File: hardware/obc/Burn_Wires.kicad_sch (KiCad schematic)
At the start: 28 parts, among them Q10 IRF7406PbF, Q20 IRLML2803, Q21 IRF7406PbF, Q4 IRLML2803, Q5 IRLML2803, Q6 MMBT2222AT, Q9 IRF7406PbF, U16 PE014006

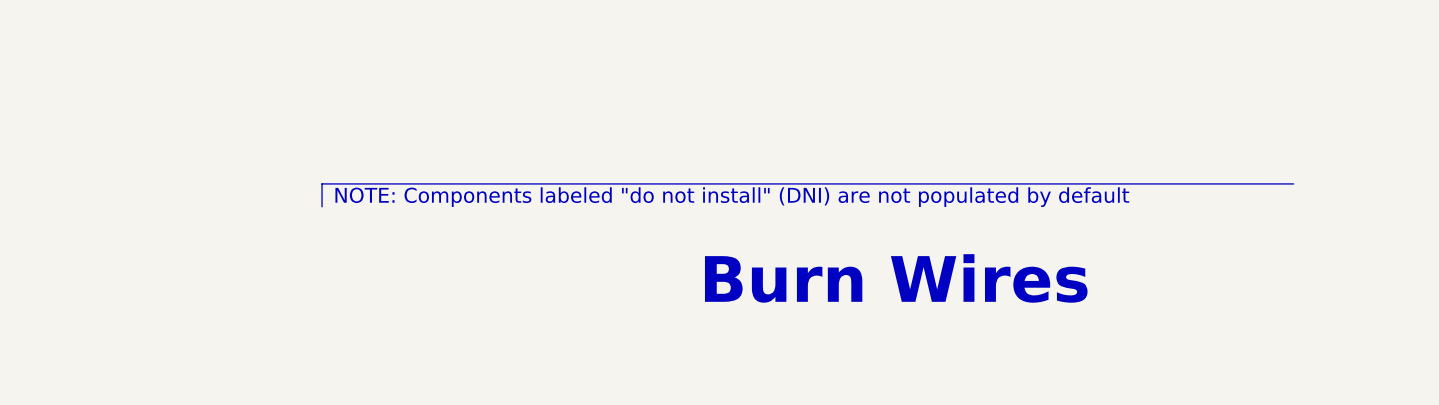
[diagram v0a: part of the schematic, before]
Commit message: obc: Schematic pages to US Letter (except Power)
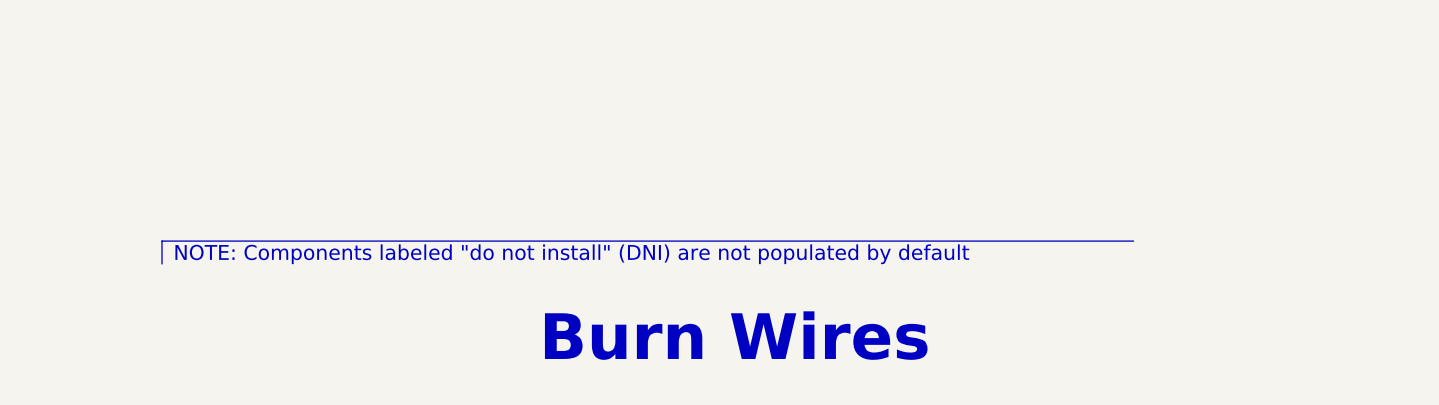
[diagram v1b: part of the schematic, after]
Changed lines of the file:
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@@
 	(generator "eeschema")
 	(generator_version "8.0")
-	(paper "A4")
+	(paper "USLetter")
 	(title_block
 		(title "PyCubed Mainboard")
@@
 	(polyline
 		(pts
-			(xy 176.53 165.1) (xy 176.53 162.56)
+			(xy 158.75 171.45) (xy 158.75 168.91)
 		)
 		(stroke
@@
 	(polyline
 		(pts
-			(xy 176.53 162.56) (xy 284.48 162.56)
+			(xy 158.75 168.91) (xy 266.7 168.91)
 		)
 		(stroke
@@
 	(text "Burn Wires"
 		(exclude_from_sim no)
-		(at 218.44 176.53 0)
+		(at 200.66 182.88 0)
 		(effects
 			(font
@@
 	(text "NOTE: Components labeled \"do not install\" (DNI) are not populated by default"
 		(exclude_from_sim no)
-		(at 177.8 165.1 0)
+		(at 160.02 171.45 0)
 		(effects
 			(font

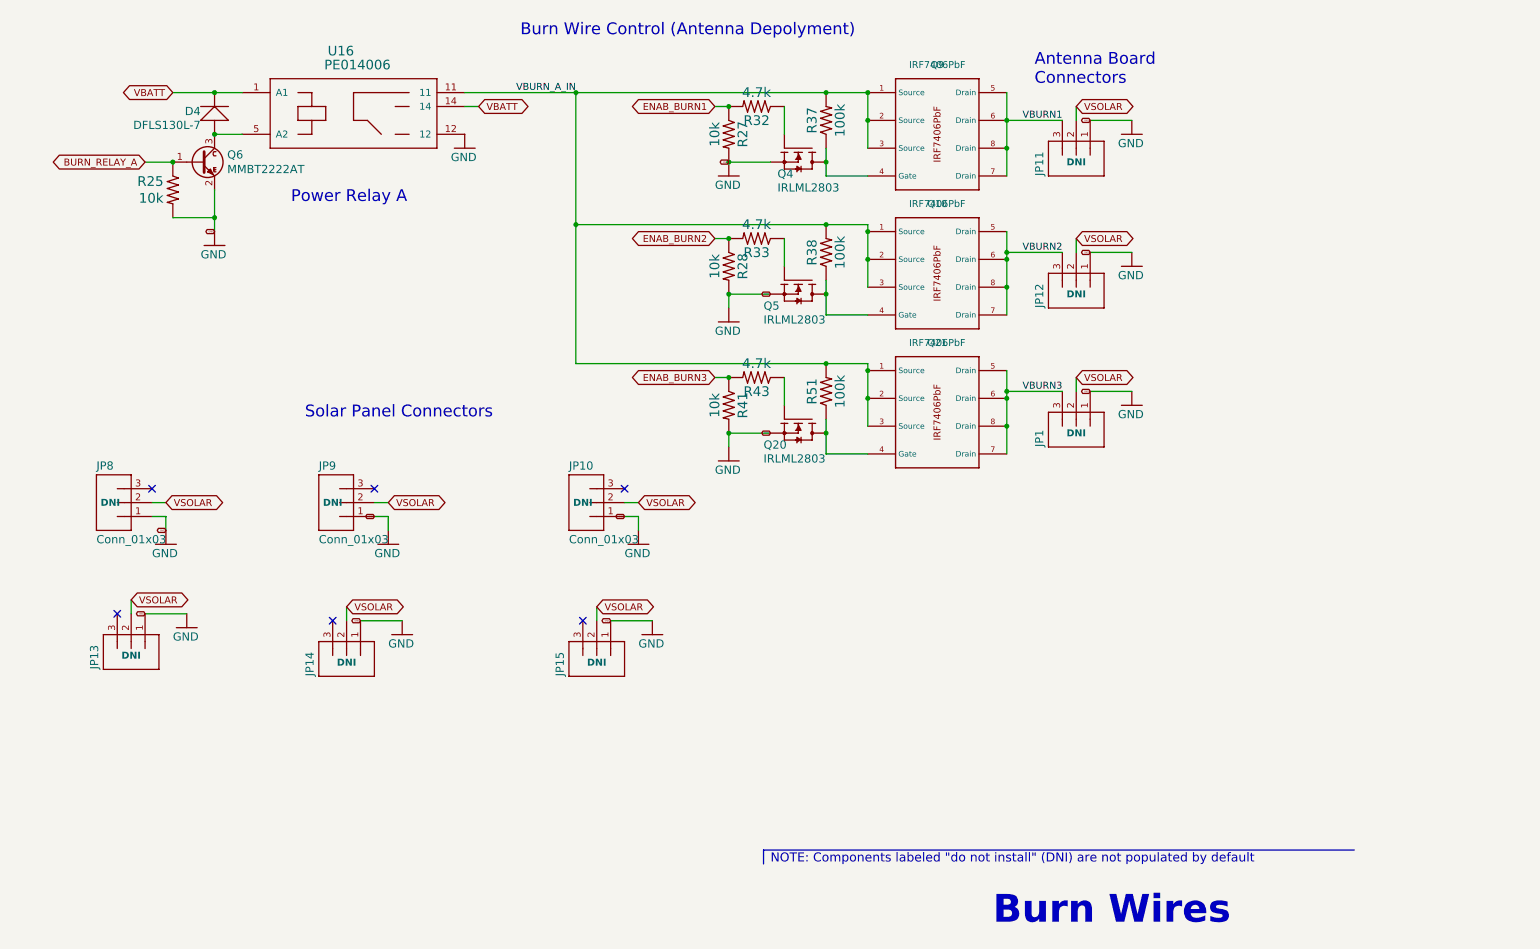
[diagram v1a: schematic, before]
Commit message: obc: schematic editing and footprint development
Deleted irrelevant SD-related circuits and pins. Created new & modified existing connector and inductor footprints. Added new components (Bat Charger, High-Rel Connector, etc.)
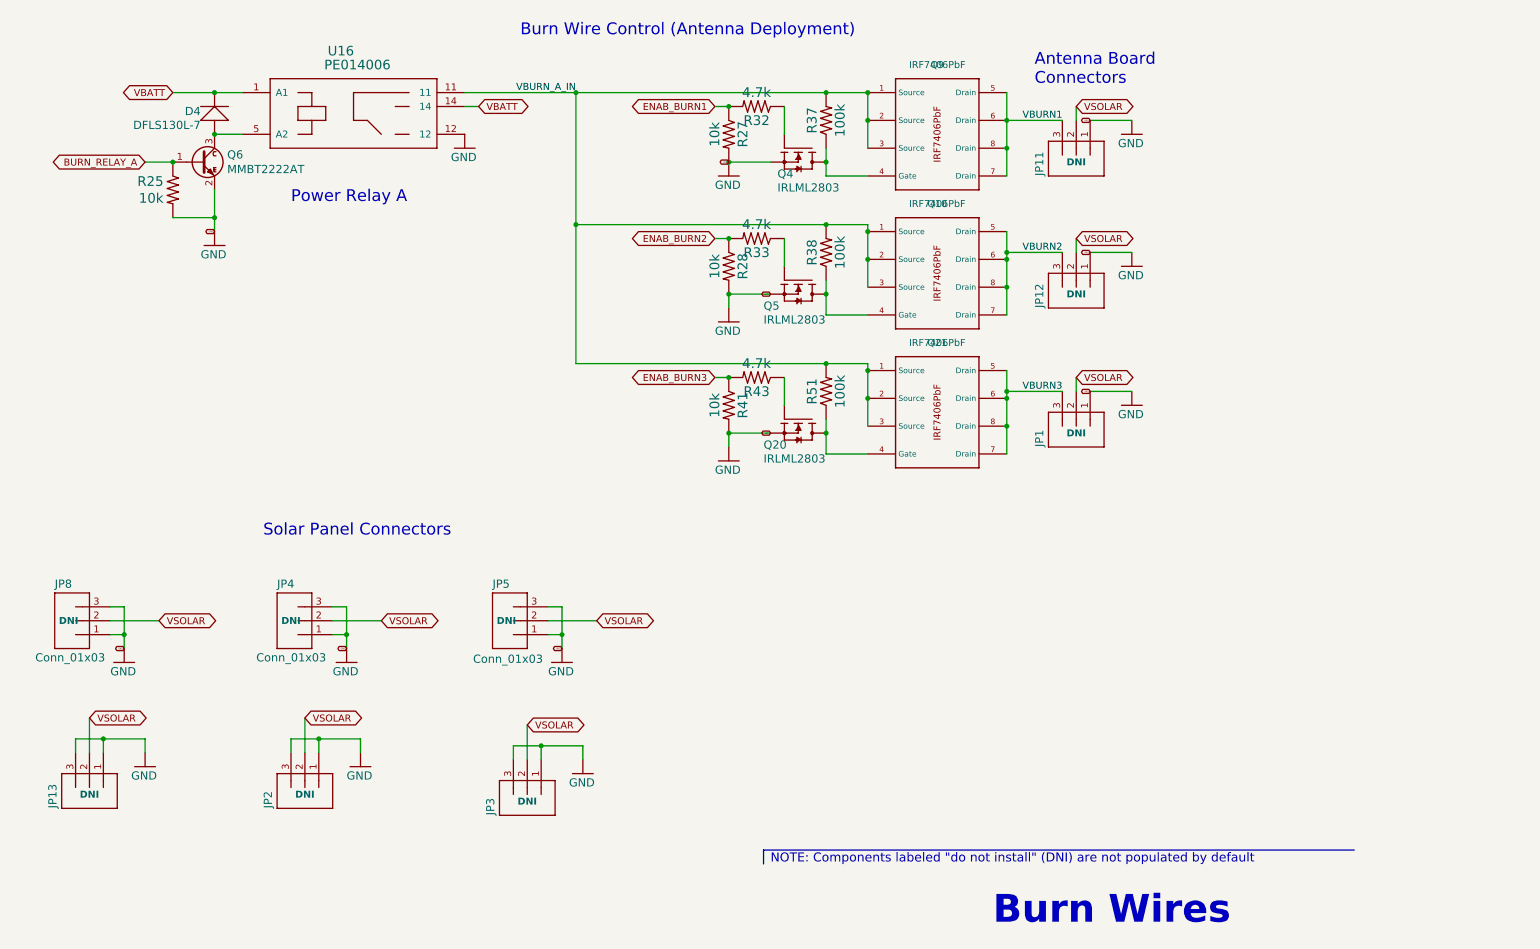
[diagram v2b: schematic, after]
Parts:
- removed JP10, JP14, JP15, JP9: Conn_01x03, mainboard:MOLEX-1X3_LOCK, symbol mainboard:M03POLAR_LOCK
- added JP2, JP3, JP4, JP5: Conn_01x03, mainboard:MOLEX-1X3_LOCK, symbol mainboard:M03POLAR_LOCK
- Q10, Q21, Q9: footprint (none) -> SSE_Footprints:SO-8_3.9x4.9mm_P1.27mm
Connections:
- net GND: now also JP13.3, JP8.3, JP2.1, JP2.3, JP3.1, JP3.3, JP4.1, JP4.3, JP5.1, JP5.3
- net VSOLAR: now also JP2.2, JP3.2, JP4.2, JP5.2
- no-connect marks 6 -> 0
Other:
- note added: "Burn Wire Control (Antenna Deployment)"
- note removed: "Burn Wire Control (Antenna Depolyment)"
- moved on the sheet: JP13, JP8

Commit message: obc: BOM component verification
Verified part numbers, availability, values, footprints, etc. of components. Next steps involve verifying footprints and potentially researching some alternative components.
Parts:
- Q10, Q21, Q9: footprint SSE_Footprints:SO-8_3.9x4.9mm_P1.27mm -> Package_SO:SO-8_3.9x4.9mm_P1.27mm
- Q20, Q4, Q5: footprint mainboard:SOT-23 -> Package_TO_SOT_SMD:SOT-23
- U16: Notes (none) -> (Potentially) Not placed by JLCPCB

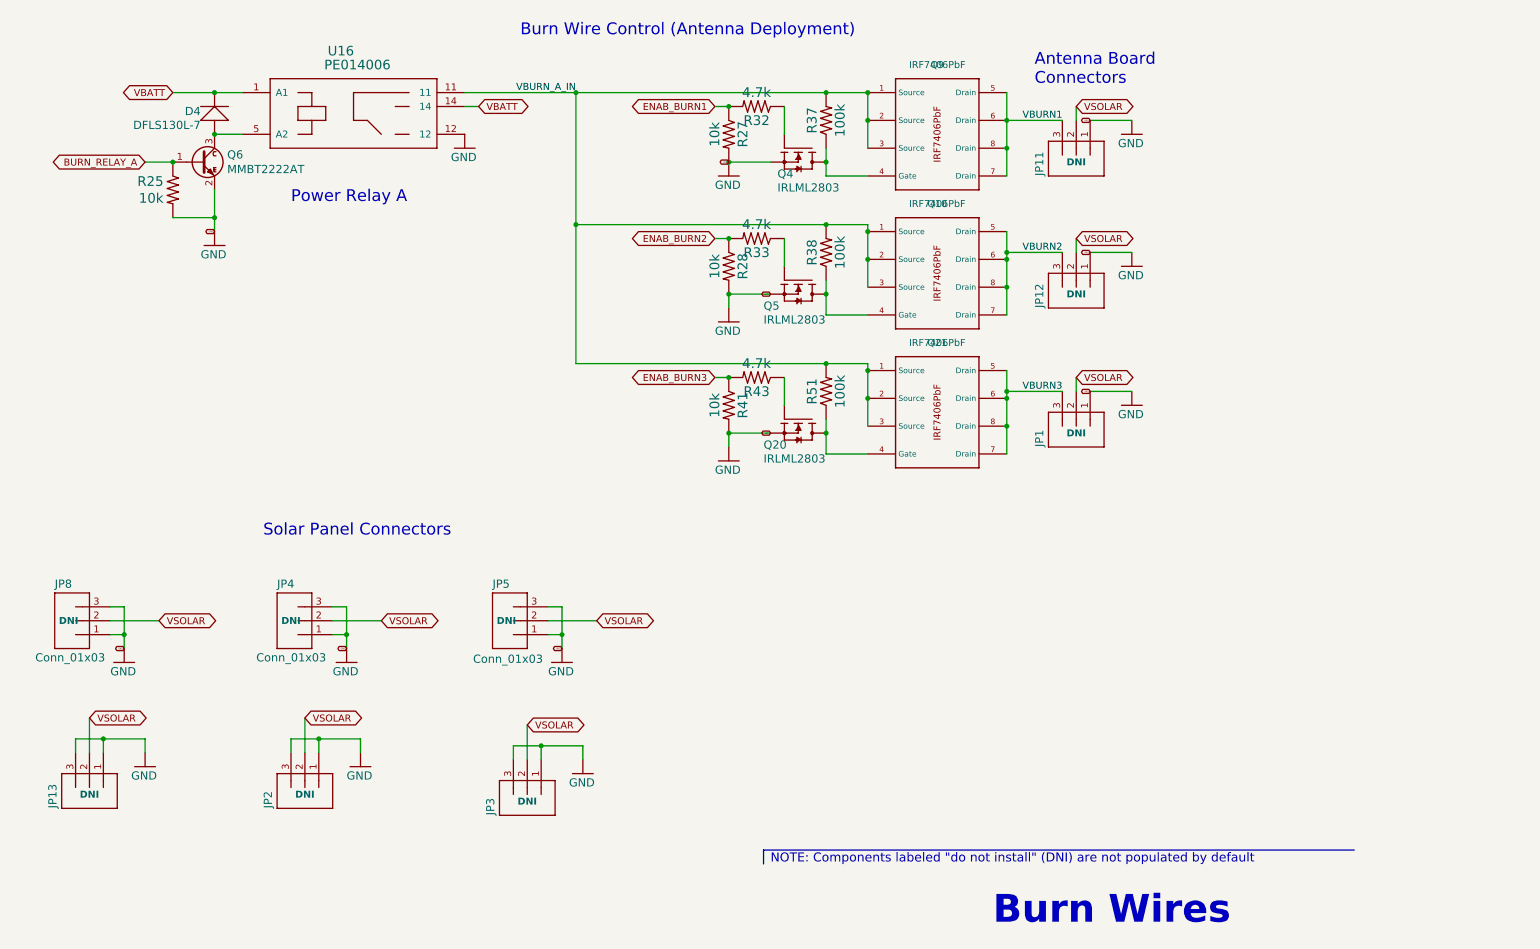
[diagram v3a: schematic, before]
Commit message: obc: footprint editing and schematic revision
Added GPS21+ and edited inductor footprints. Edited schematic circuitry and re-annotated schematic components.
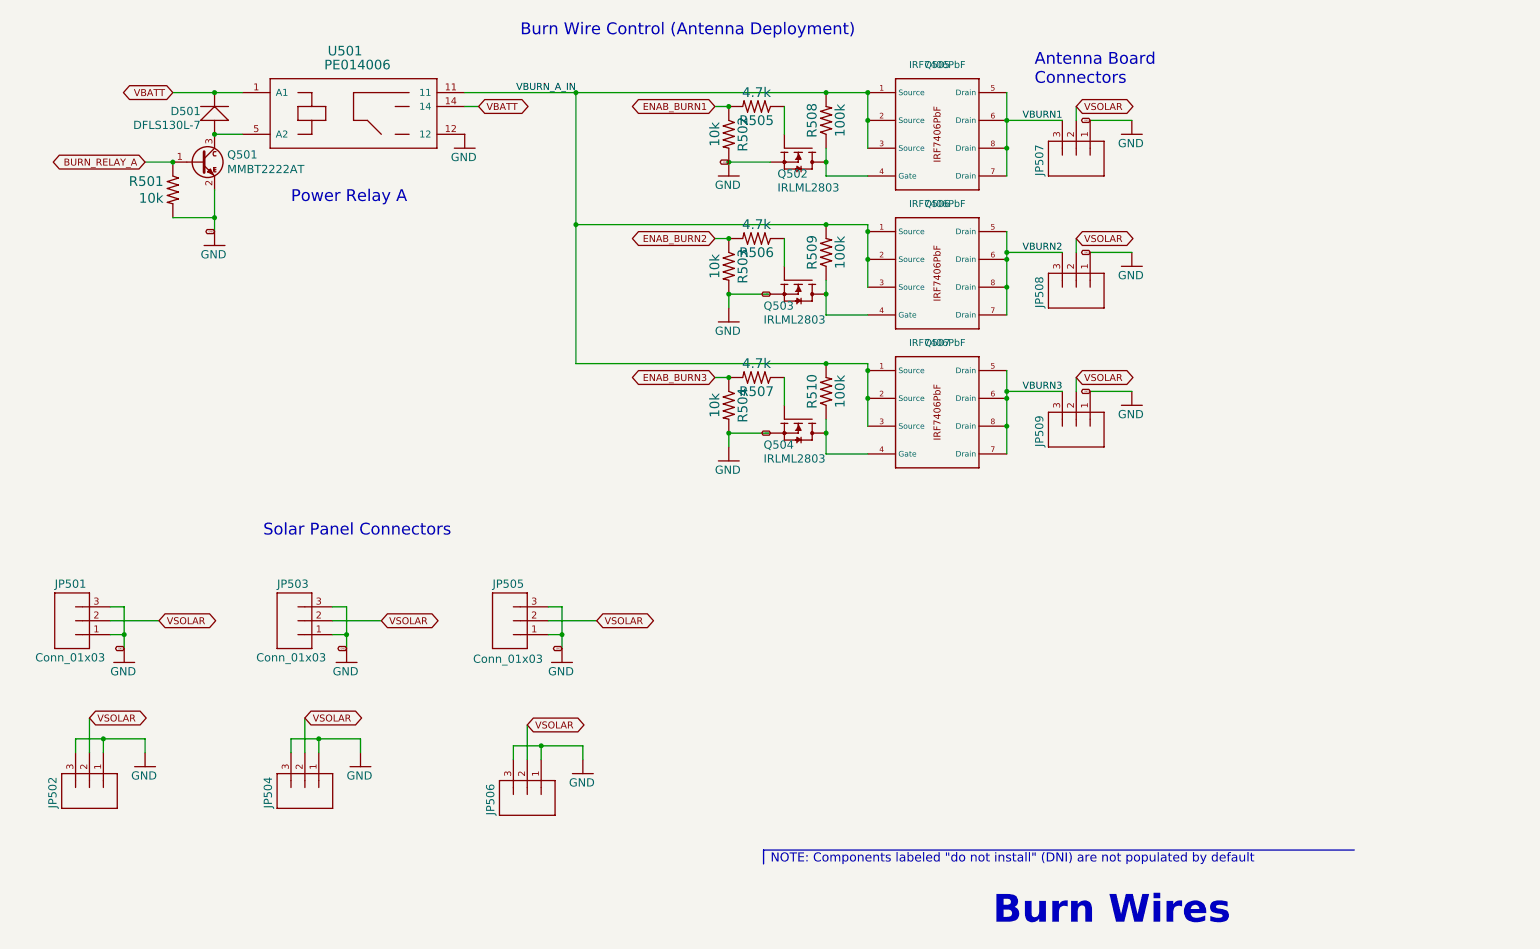
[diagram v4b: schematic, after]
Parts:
- JP501: renamed from JP8; DNI DNI -> (none); LCSC NotAvailable -> (none)
- JP502: renamed from JP13; DNI DNI -> (none); LCSC NotAvailable -> (none)
- JP503: renamed from JP4; DNI DNI -> (none); LCSC NotAvailable -> (none)
- JP504: renamed from JP2; DNI DNI -> (none); LCSC NotAvailable -> (none)
- JP505: renamed from JP5; DNI DNI -> (none); LCSC NotAvailable -> (none)
- JP506: renamed from JP3; DNI DNI -> (none); LCSC NotAvailable -> (none)
- JP507: renamed from JP11; DNI DNI -> (none); LCSC NotAvailable -> (none)
- JP508: renamed from JP12; DNI DNI -> (none); LCSC NotAvailable -> (none)
- JP509: renamed from JP1; DNI DNI -> (none); LCSC NotAvailable -> (none)
- renumbered D4 to D501, Q6 to Q501, Q4 to Q502, Q5 to Q503, Q20 to Q504, Q9 to Q505, Q10 to Q506, Q21 to Q507, R25 to R501, R27 to R502, R28 to R503, R41 to R504, R32 to R505, R33 to R506, R43 to R507, R37 to R508, R38 to R509, R51 to R510, U16 to U501

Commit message: obc: BOM editing
Edited the DNI status of several components to be more reflective of our obc setup plans.
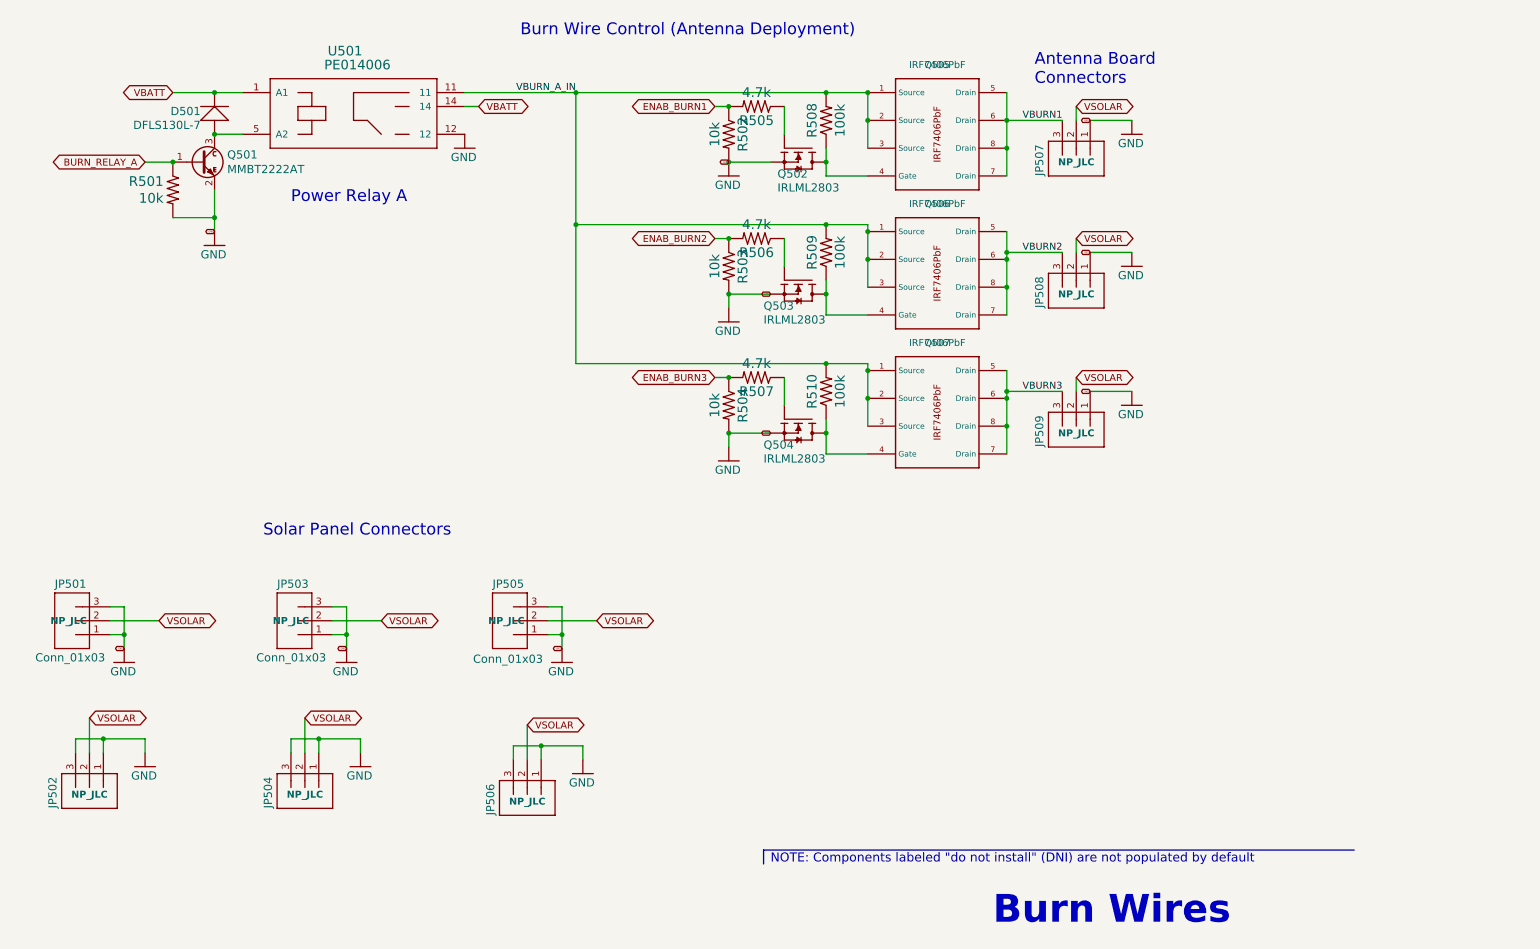
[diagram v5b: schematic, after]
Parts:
- JP501, JP502, JP503, JP504, JP505, JP506, JP507, JP508, JP509: DNI (none) -> NP_JLC
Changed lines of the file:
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@@
 			)
 		)
-		(property "DNI" ""
+		(property "DNI" "NP_JLC"
 			(at 215.9 67.31 90)
 			(effects
@@
 			)
 		)
-		(property "DNI" ""
+		(property "DNI" "NP_JLC"
 			(at 215.9 43.18 90)
 			(effects
@@
 			)
 		)
-		(property "DNI" ""
+		(property "DNI" "NP_JLC"
 			(at 35.56 158.75 90)
 			(effects
@@
 			)
 		)
-		(property "DNI" ""
+		(property "DNI" "NP_JLC"
 			(at 31.75 127 0)
 			(effects
@@
 			)
 		)
-		(property "DNI" ""
+		(property "DNI" "NP_JLC"
 			(at 215.9 92.71 90)
 			(effects
@@
 			)
 		)
-		(property "DNI" ""
+		(property "DNI" "NP_JLC"
 			(at 74.93 158.75 90)
 			(effects
@@
 			)
 		)
-		(property "DNI" ""
+		(property "DNI" "NP_JLC"
 			(at 115.57 160.02 90)
 			(effects
@@
 			)
 		)
-		(property "DNI" ""
+		(property "DNI" "NP_JLC"
 			(at 111.76 127 0)
 			(effects
@@
 			)
 		)
-		(property "DNI" ""
+		(property "DNI" "NP_JLC"
 			(at 72.39 127 0)
 			(effects
